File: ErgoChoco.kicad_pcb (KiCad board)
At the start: 2 copper layers, 262 x 112 mm, 159 parts, among them J1 USB_B_Micro, Q1 Q_NPN_BCE, SW1 SW_Push, U1 ATmega32U4-AU, U2 PRTR5V0U2X, Y1 16MHz

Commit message: late updates before asking Reddit for help
-remove tooling holes again
-rename BOM and add JLCPCB BOM + CPL
-update readme to include layout explanation
-add gerbers
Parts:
- removed the REF** at (276.4, 52.5)
- removed the REF** at (168.9, 159.5)
- removed the REF** at (128.0, 159.5)
- removed e: JLCPCB_tooling_hole, Choco617_parts:JLCPCB_tooling_hole
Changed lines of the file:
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@@
     (tracks 1410)
     (zones 0)
-    (modules 159)
+    (modules 155)
     (nets 126)
   )
@@
     (solder_mask_min_width 0.12)
     (aux_axis_origin 0 0)
-    (visible_elements 7FF7EFFF)
+    (visible_elements 7FFFEFFF)
     (pcbplotparams
-      (layerselection 0x010fc_ffffffff)
+      (layerselection 0x01000_7fffffff)
       (usegerberextensions false)
       (usegerberattributes true)
       (usegerberadvancedattributes true)
       (creategerberjobfile true)
-      (excludeedgelayer true)
-      (linewidth 0.100000)
+      (excludeedgelayer false)
+      (linewidth 0.150000)
       (plotframeref false)
       (viasonmask false)
@@
       (psa4output false)
       (plotreference true)
-      (plotvalue true)
+      (plotvalue false)
       (plotinvisibletext false)
       (padsonsilk false)
       (subtractmaskfromsilk false)
-      (outputformat 1)
+      (outputformat 3)
       (mirror false)
-      (drillshape 1)
+      (drillshape 0)
       (scaleselection 1)
-      (outputdirectory ""))
+      (outputdirectory "./"))
   )
   (net 0 "")
@@
     (add_net VCC)
   )
-  (module Choco617_parts:JLCPCB_tooling_hole (layer F.Cu)
-    (at 276.43125 52.5)
-    (fp_text reference REF** (at 0 0.5) (layer F.SilkS)
-      (effects (font (size 1 1) (thickness 0.15)))
-    )
-    (fp_text value JLCPCB_tooling_hole (at 0 -0.5) (layer F.Fab)
-      (effects (font (size 1 1) (thickness 0.15)))
-    )
-    (pad "" np_thru_hole circle (at 0 0) (size 1.3 1.3) (drill 1.152) (layers *.Cu *.Mask))
-  )
-  (module Choco617_parts:JLCPCB_tooling_hole (layer F.Cu)
-    (at 168.8625 159.5)
-    (fp_text reference REF** (at 0 0.5) (layer F.SilkS)
-      (effects (font (size 1 1) (thickness 0.15)))
-    )
-    (fp_text value JLCPCB_tooling_hole (at 0 -0.5) (layer F.Fab)
-      (effects (font (size 1 1) (thickness 0.15)))
-    )
-    (pad "" np_thru_hole circle (at 0 0) (size 1.3 1.3) (drill 1.152) (layers *.Cu *.Mask))
-  )
-  (module Choco617_parts:JLCPCB_tooling_hole (layer F.Cu)
-    (at 128 159.5)
-    (fp_text reference REF** (at 0 0.5) (layer F.SilkS)
-      (effects (font (size 1 1) (thickness 0.15)))
-    )
-    (fp_text value JLCPCB_tooling_hole (at 0 -0.5) (layer F.Fab)
-      (effects (font (size 1 1) (thickness 0.15)))
-    )
-    (pad "" np_thru_hole circle (at 0 0) (size 1.3 1.3) (drill 1.152) (layers *.Cu *.Mask))
-  )
-  (module Choco617_parts:JLCPCB_tooling_hole (layer F.Cu)
-    (at 20.43125 52.5)
-    (fp_text reference e (at 0 0.5) (layer F.SilkS)
-      (effects (font (size 1 1) (thickness 0.15)))
-    )
-    (fp_text value JLCPCB_tooling_hole (at 0 -0.5) (layer F.Fab)
-      (effects (font (size 1 1) (thickness 0.15)))
-    )
-    (pad "" np_thru_hole circle (at 0 0) (size 1.3 1.3) (drill 1.152) (layers *.Cu *.Mask))
-  )
   (module Choco617_parts:Kailh_socket_MX_PCBmount_LED_1U (layer F.Cu)

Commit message: started deleting things from integrated MCU
-deleted traces and edge cuts in pcbnew
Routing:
- net +5V: track 1194.7 -> 0.00 mm, vias 37 -> 0
- net LEDGND: track 956.1 -> 0.00 mm, vias 10 -> 0
- net ROW2: track 300.4 -> 0.00 mm, vias 2 -> 0
- net ROW0: track 298.4 -> 0.00 mm, vias 4 -> 0
- net ROW1: track 289.0 -> 0.00 mm, vias 4 -> 0
- net COL0: track 202.6 -> 0.00 mm, vias 1 -> 0
- net COL11: track 193.8 -> 0.00 mm, vias 5 -> 0
- net ROW3: track 192.8 -> 0.00 mm, vias 2 -> 0
- net COL1: track 185.9 -> 0.00 mm, vias 1 -> 0
- net COL2: track 178.1 -> 0.00 mm, vias 3 -> 0
- net COL10: track 173.1 -> 0.00 mm, vias 5 -> 0
- net COL3: track 166.1 -> 0.00 mm, vias 1 -> 0
- net COL9: track 164.8 -> 0.00 mm, vias 5 -> 0
- net COL8: track 117.8 -> 0.00 mm, vias 3 -> 0
- net COL4: track 112.7 -> 0.00 mm, vias 1 -> 0
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- removed copper zone on B.Cu, net GND
- removed copper zone on F.Cu, net GND
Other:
- board size 262 x 112 mm -> 5.1 x 0.8 mm
- board text removed: "ErgoChoco v1.0"
- board text removed: "designed by u/Choco617"
- board text removed: "https://github.com/Choco617/ErgoChoco-PCB"

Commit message: introduced Pro Micro
-put Pro Micro into schematic
-updated PCB from schematic
-moved all switches 10mm farther apart
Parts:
- removed C1: 1uF, Capacitor_SMD:C_0805_2012Metric
- removed C2, C3, C4: 0.1uF, Capacitor_SMD:C_0805_2012Metric
- removed C5: 10uF, Capacitor_SMD:C_0805_2012Metric
- removed C6, C7: 22pF, Capacitor_SMD:C_0805_2012Metric
- removed F1: 500mA, Fuse:Fuse_1206_3216Metric
- removed J1: USB_B_Micro, Choco617_parts:CUI_UJ2-MIBH2-4-SMT
- removed R43, R46: 10k, Resistor_SMD:R_0805_2012Metric
- removed R44, R45: 22, Resistor_SMD:R_0805_2012Metric
- removed REF** (x10): NPTH_2.2_4, Choco617_parts:NPTH_2.2_4
- removed SW1: SW_Push, random-keyboard-parts:SKQG-1155865
- removed U2: PRTR5V0U2X, random-keyboard-parts:SOT143B
- removed Y1: 16MHz, Crystal:Crystal_SMD_3225-4Pin_3.2x2.5mm
- U1: value ATmega32U4-AU -> ProMicro; footprint Package_QFP:TQFP-44_10x10mm_P0.8mm -> Keebio-Parts:ArduinoProMicro; moved to B.Cu
- moved D39 103.6 mm to (125.5, 49.7), turned to 75 degrees
- moved R39 102.6 mm to (124.0, 55.2), turned to 75 degrees
- moved D40 95.2 mm to (175.3, 45.0), turned to 105 degrees
- moved R40 93.9 mm to (176.6, 49.9), turned to 105 degrees
- moved D38 91.7 mm to (117.2, 46.1), turned to 75 degrees
- moved R38 91.2 mm to (115.9, 51.3), turned to 75 degrees
- moved D41 85.3 mm to (182.6, 44.2), turned to 105 degrees
- moved R41 84.1 mm to (183.8, 49.9), turned to 105 degrees
- moved D42 83.9 mm to (190.2, 42.3)
- moved R42 83.9 mm to (191.5, 47.1)
- moved D37 83.1 mm to (110.4, 45.0)
- moved R37 83.1 mm to (109.1, 49.8)
- moved R30 79.2 mm to (96.6, 49.5), turned to 75 degrees
- moved R18 78.2 mm to (98.9, 36.1)
- moved D18 78.2 mm to (100.1, 31.3)
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- renumbered MX1 to MXe
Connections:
- U1 pad 10: ROW1 -> Net-(U1-Pad10)
- U1 pad 11: ROW0 -> Net-(U1-Pad11)
- U1 pad 14: +5V -> Net-(U1-Pad14)
- U1 pad 15: GND -> Net-(U1-Pad15)
- U1 pad 2: +5V -> Net-(U1-Pad2)
- U1 pad 23: GND -> Net-(U1-Pad23)
- U1 pad 24: +5V -> Net-(U1-Pad24)
- U1 pad 3: D- -> Net-(U1-Pad3)
- U1 pad 4: D+ -> Net-(U1-Pad4)
- U1 pad 5: GND -> Net-(U1-Pad5)
- U1 pad 7: +5V -> Net-(U1-Pad7)
- U1 pad 8: ROW3 -> Net-(U1-Pad8)
- U1 pad 9: ROW2 -> Net-(U1-Pad9)
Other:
- board outline removed

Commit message: routed columns
-routed columns together (not to Pro Micro yet)
-flipped diodes and resistors to back side of board
-added calculator for figuring out weird angles of traces
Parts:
- removed MXe: MX-LED, Choco617_parts:Kailh_socket_MX_PCBmount_LED_1U
- added MX1: MX-LED, Choco617_parts:Kailh_socket_MX_PCBmount_LED_1U, F.Cu at (34.3, 64.0)
- D1, D10, D11, D12, D13, D14, D15, D16, D17, D18, D19, D2, D20, D21, D22, D23, D24, D25, D26, D27, D28, D29, D3, D30, D31, D32, D33, D34, D35, D36, D37, D38, D39, D4, D40, D41, D42, D5, D6, D7, D8, D9: footprint Diode_SMD:D_SOD-123 -> Choco617_parts:D_SOD-123-HandSolder; moved to B.Cu
- R1, R10, R11, R12, R13, R14, R15, R16, R17, R18, R19, R2, R20, R21, R22, R23, R24, R25, R26, R27, R28, R29, R3, R30, R31, R32, R33, R34, R35, R36, R37, R38, R39, R4, R40, R41, R42, R5, R6, R7, R8, R9: moved to B.Cu
- moved R1 45.3 mm to (37.1, 70.0), turned to 345 degrees
- moved D1 35.4 mm to (32.5, 50.7), turned to 345 degrees
- moved R40 22.5 mm to (178.6, 27.5), turned to 270 degrees
- moved R41 21.5 mm to (184.3, 28.4), turned to 270 degrees
- moved R39 20.0 mm to (122.3, 35.3), turned to 270 degrees
- moved R42 16.3 mm to (193.0, 30.9), turned to 270 degrees
- moved R13 14.8 mm to (45.2, 25.5), turned to 270 degrees
- moved R19 14.6 mm to (197.9, 13.0), turned to 270 degrees
- moved R31 14.2 mm to (201.6, 31.6), turned to 270 degrees
- moved R25 13.2 mm to (43.7, 38.5), turned to 270 degrees
- moved D40 12.9 mm to (178.6, 32.5), turned to 270 degrees
- moved R26 12.4 mm to (54.4, 39.1), turned to 270 degrees
- moved R7 12.1 mm to (198.2, -0.49), turned to 270 degrees
- moved R38 12.1 mm to (115.0, 39.3), turned to 270 degrees
- moved R14 11.9 mm to (55.7, 26.9), turned to 270 degrees
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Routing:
- net COL6: track 0.00 -> 74.2 mm
- net COL5: track 0.00 -> 70.3 mm
- net COL7: track 0.00 -> 68.1 mm
- net COL3: track 0.00 -> 66.7 mm
- net COL8: track 0.00 -> 66.7 mm
- net COL4: track 0.00 -> 63.2 mm
- net COL2: track 0.00 -> 38.0 mm
- net COL9: track 0.00 -> 38.0 mm
- net COL1: track 0.00 -> 38.0 mm
- net COL11: track 0.00 -> 38.0 mm
- net COL10: track 0.00 -> 38.0 mm
- net COL0: track 0.00 -> 38.0 mm
- net Net-(MX1-Pad4): track 0.00 -> 1.99 mm

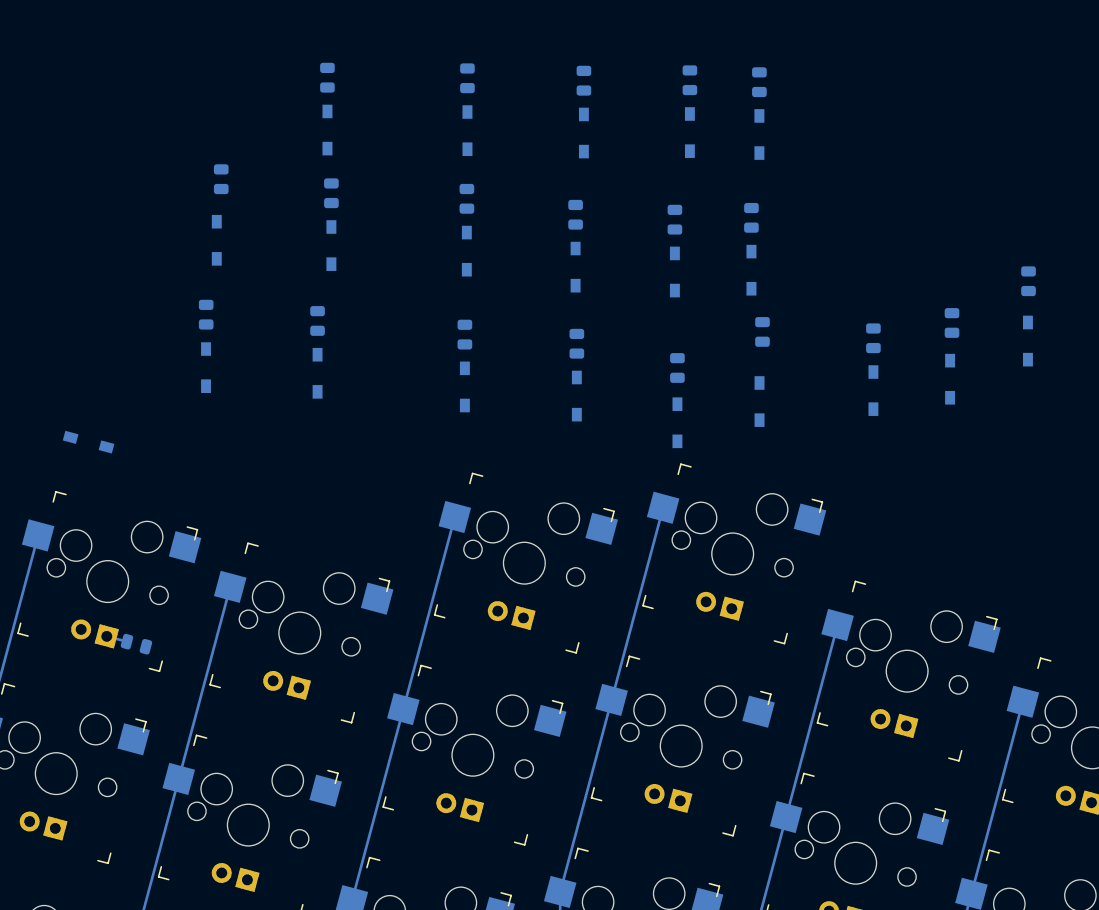
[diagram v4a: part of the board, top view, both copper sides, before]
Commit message: routed LH top row
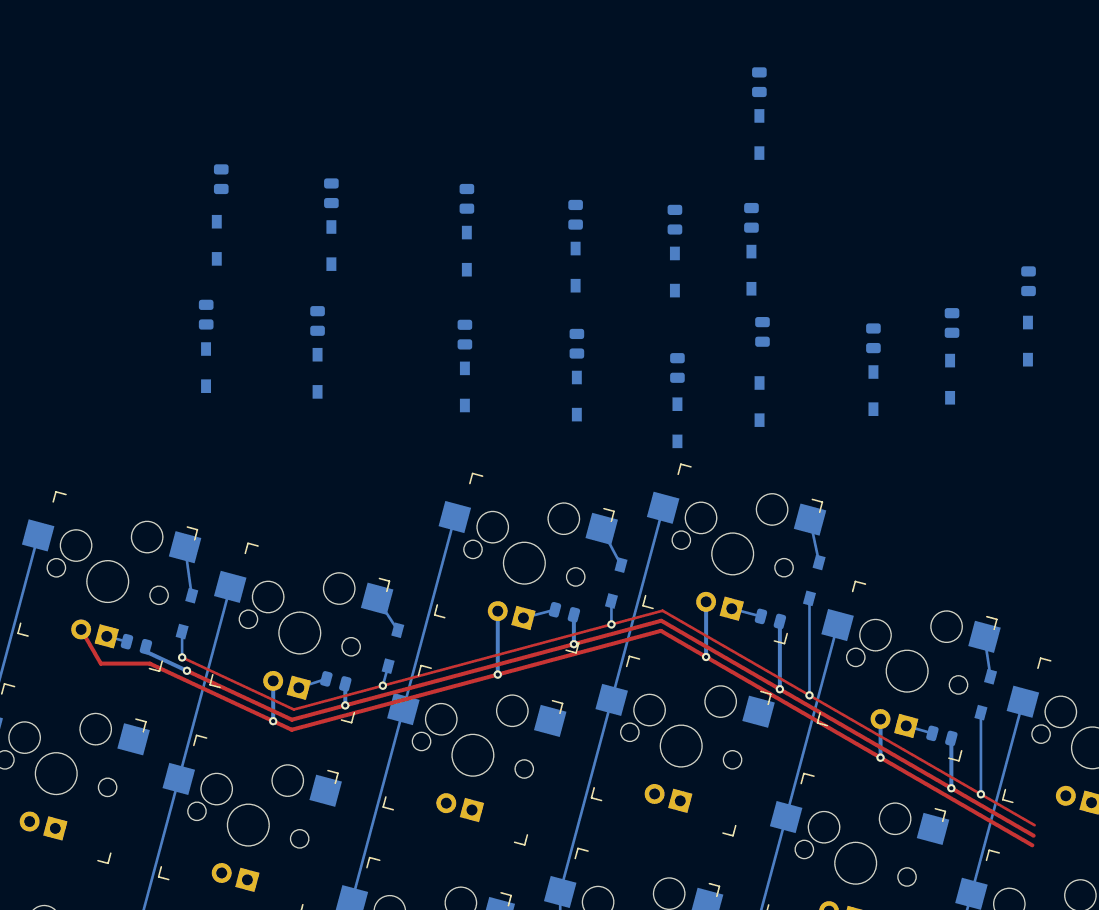
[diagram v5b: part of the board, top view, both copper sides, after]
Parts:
- moved R5 67.1 mm to (114.0, 78.7), turned to 345 degrees
- moved D5 60.7 mm to (118.2, 74.8), turned to 75 degrees
- moved R2 57.7 mm to (56.1, 73.5), turned to 345 degrees
- moved R4 54.4 mm to (97.7, 67.6), turned to 345 degrees
- moved R3 51.9 mm to (78.0, 66.9), turned to 345 degrees
- moved D2 49.9 mm to (61.6, 70.4), turned to 75 degrees
- moved D4 48.1 mm to (101.9, 63.9), turned to 75 degrees
- moved D3 45.5 mm to (82.9, 64.1), turned to 75 degrees
- moved D1 18.9 mm to (41.9, 67.1), turned to 75 degrees
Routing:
- net +5V: track 0.00 -> 119.8 mm, vias 0 -> 4
- net ROW0: track 0.00 -> 112.7 mm, vias 0 -> 5
- net LEDGND: track 0.00 -> 109.1 mm, vias 0 -> 5
- net Net-(D1-Pad2): track 0.00 -> 4.67 mm
- net Net-(D4-Pad2): track 0.00 -> 4.19 mm
- net Net-(D3-Pad2): track 0.00 -> 3.93 mm
- net Net-(D5-Pad2): track 0.00 -> 3.86 mm
- net Net-(D2-Pad2): track 0.00 -> 3.60 mm
- net Net-(MX3-Pad4): track 0.00 -> 3.11 mm
- net Net-(MX4-Pad4): track 0.00 -> 2.88 mm
- net Net-(MX2-Pad4): track 0.00 -> 2.76 mm
- net Net-(MX5-Pad4): track 0.00 -> 2.60 mm

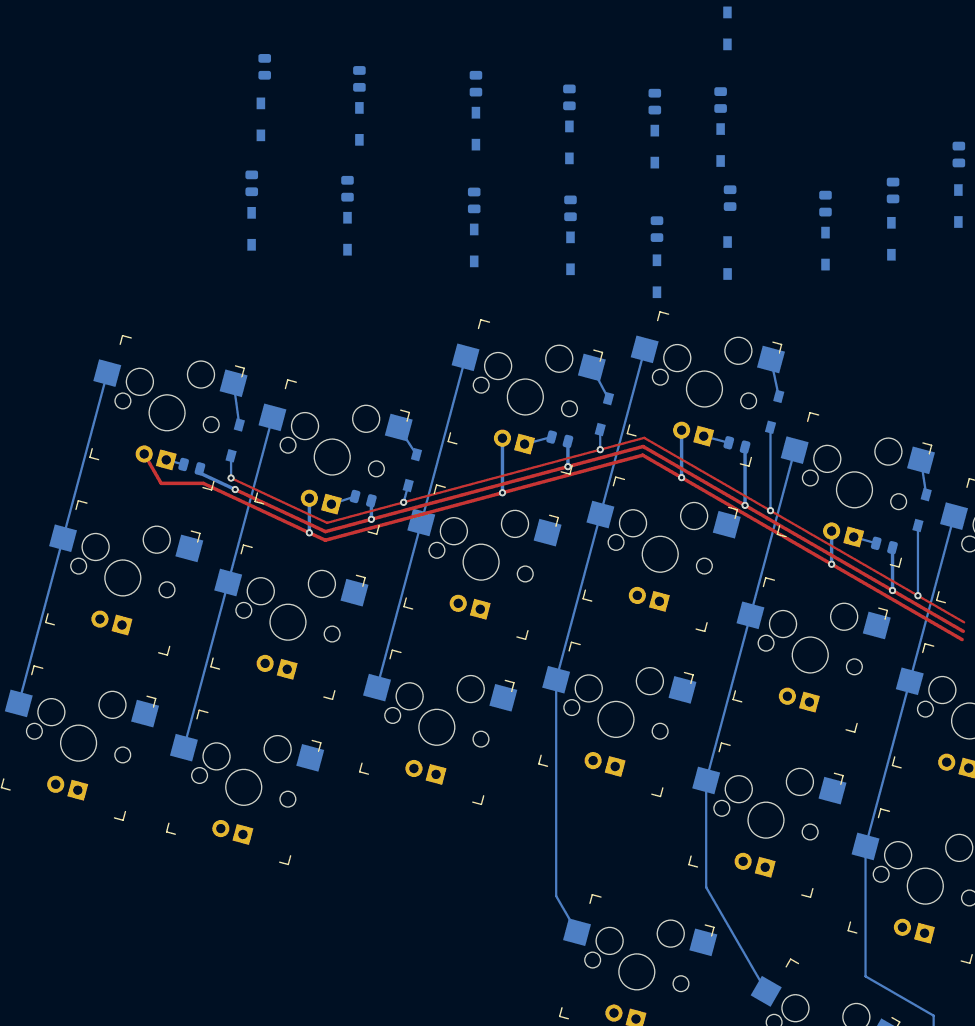
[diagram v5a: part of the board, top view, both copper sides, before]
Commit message: routed other two LH rows
-still excluding innermost row and thumb cluster for now
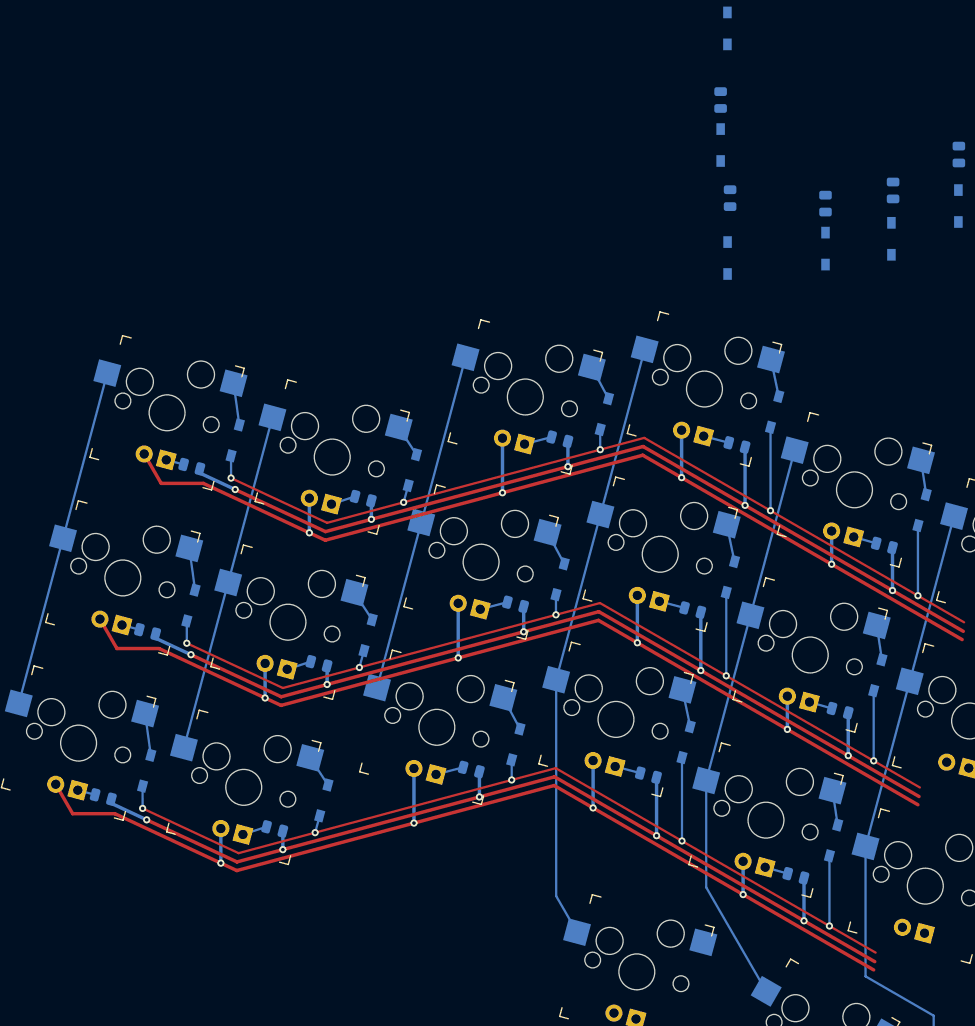
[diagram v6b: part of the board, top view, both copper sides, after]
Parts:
- moved R29 73.5 mm to (104.2, 115.4), turned to 345 degrees
- moved R26 71.6 mm to (46.3, 110.2), turned to 345 degrees
- moved R17 70.7 mm to (109.1, 97.1), turned to 345 degrees
- moved R25 70.2 mm to (27.2, 106.7), turned to 345 degrees
- moved D29 65.7 mm to (108.4, 111.5), turned to 75 degrees
- moved R14 65.2 mm to (51.2, 91.9), turned to 345 degrees
- moved R13 64.1 mm to (32.2, 88.3), turned to 345 degrees
- moved D17 63.8 mm to (113.3, 93.2), turned to 75 degrees
- moved R28 63.6 mm to (87.8, 104.3), turned to 345 degrees
- moved R27 63.2 mm to (68.1, 103.6), turned to 345 degrees
- moved D26 63.0 mm to (51.8, 107.1), turned to 75 degrees
- moved D25 61.3 mm to (32.1, 103.8), turned to 75 degrees
- moved R16 58.6 mm to (92.7, 85.9), turned to 345 degrees
- moved R15 58.0 mm to (73.1, 85.3), turned to 345 degrees
- moved D14 56.8 mm to (56.7, 88.7), turned to 75 degrees
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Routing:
- net +5V: track 119.8 -> 359.3 mm, vias 4 -> 12
- net LEDGND: track 109.1 -> 327.3 mm, vias 5 -> 15
- net ROW2: track 0.00 -> 113.0 mm, vias 0 -> 5
- net ROW1: track 0.00 -> 113.0 mm, vias 0 -> 5
- net Net-(D25-Pad2): track 0.00 -> 4.67 mm
- net Net-(D13-Pad2): track 0.00 -> 4.67 mm
- net Net-(D28-Pad2): track 0.00 -> 4.18 mm
- net Net-(D16-Pad2): track 0.00 -> 4.18 mm
- net Net-(D15-Pad2): track 0.00 -> 3.93 mm
- net Net-(D27-Pad2): track 0.00 -> 3.93 mm
- net Net-(D17-Pad2): track 0.00 -> 3.86 mm
- net Net-(D29-Pad2): track 0.00 -> 3.86 mm
- net Net-(D26-Pad2): track 0.00 -> 3.60 mm
- net Net-(D14-Pad2): track 0.00 -> 3.60 mm
- net Net-(MX27-Pad4): track 0.00 -> 3.11 mm
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
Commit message: routed right hand and thumb arcs
-still haven't routed innermost column on left hand
-need to establish Pro Micro location and edge cuts first
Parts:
- moved R40 120.1 mm to (180.6, 147.6), turned to 45 degrees
- moved R39 118.6 mm to (122.6, 153.9), turned to 315 degrees
- moved D39 113.5 mm to (129.4, 154.3), turned to 45 degrees
- moved R41 108.8 mm to (197.1, 136.4), turned to 30 degrees
- moved D40 108.0 mm to (180.5, 140.5), turned to 135 degrees
- moved R38 101.8 mm to (107.4, 140.8), turned to 330 degrees
- moved R42 101.7 mm to (215.9, 129.9), turned to 15 degrees
- moved D41 96.5 mm to (198.9, 129.7), turned to 120 degrees
- moved D38 94.5 mm to (113.9, 139.2), turned to 60 degrees
- moved R37 93.2 mm to (89.4, 132.2), turned to 345 degrees
- moved D42 91.7 mm to (219.5, 123.7), turned to 105 degrees
- moved R19 90.8 mm to (179.4, 101.9), turned to 15 degrees
- moved R31 90.3 mm to (184.3, 120.3), turned to 15 degrees
- moved R7 87.3 mm to (174.5, 83.6), turned to 15 degrees
- moved R30 86.1 mm to (121.5, 122.7), turned to 345 degrees
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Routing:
- net +5V: track 359.3 -> 982.7 mm, vias 12 -> 36
- net LEDGND: track 327.3 -> 909.7 mm, vias 15 -> 39
- net ROW3: track 0.00 -> 169.8 mm, vias 0 -> 6
- net ROW0: track 112.7 -> 263.8 mm, vias 5 -> 11
- net ROW1: track 113.0 -> 264.1 mm, vias 5 -> 11
- net ROW2: track 113.0 -> 264.1 mm, vias 5 -> 11
- net Net-(D39-Pad2): track 0.00 -> 5.00 mm
- net Net-(D23-Pad2): track 0.00 -> 4.99 mm
- net Net-(D11-Pad2): track 0.00 -> 4.99 mm
- net Net-(D35-Pad2): track 0.00 -> 4.99 mm
- net Net-(D36-Pad2): track 0.00 -> 4.99 mm
- net Net-(D24-Pad2): track 0.00 -> 4.99 mm
- net Net-(D12-Pad2): track 0.00 -> 4.99 mm
- net Net-(D38-Pad2): track 0.00 -> 4.69 mm
- net Net-(D37-Pad2): track 0.00 -> 4.66 mm
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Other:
- board text removed: "repo:"
